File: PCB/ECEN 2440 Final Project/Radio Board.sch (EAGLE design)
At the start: 12 parts

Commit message: minor changes to board
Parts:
- added JP3: (no value), pinhead:PINHD-1X2
- added U$5: LDO-S-816, Custom Library:LDO-S-816
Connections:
- new net VCC: JP3.2, U$5.P$5
- net GND: now also JP3.1, U$5.P$2
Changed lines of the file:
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@@
 <part name="SJ1" library="jumper" library_urn="urn:adsk.eagle:library:252" deviceset="SJ" device="" package3d_urn="urn:adsk.eagle:package:15471/1"/>
 <part name="JP1" library="pinhead" library_urn="urn:adsk.eagle:library:325" deviceset="PINHD-1X1" device="" package3d_urn="urn:adsk.eagle:package:22485/2"/>
+<part name="U$5" library="Custom Library" deviceset="LDO-S-816" device=""/>
+<part name="GND16" library="supply1" library_urn="urn:adsk.eagle:library:371" deviceset="GND" device=""/>
+<part name="JP3" library="pinhead" library_urn="urn:adsk.eagle:library:325" deviceset="PINHD-1X2" device="" package3d_urn="urn:adsk.eagle:package:22435/2"/>
+<part name="GND2" library="supply1" library_urn="urn:adsk.eagle:library:371" deviceset="GND" device=""/>
+<part name="P+1" library="supply1" library_urn="urn:adsk.eagle:library:371" deviceset="VCC" device=""/>
 </parts>
 <sheets>
@@
 <attribute name="VALUE" x="95.25" y="12.7" size="1.778" layer="96"/>
 </instance>
+<instance part="U$5" gate="G$1" x="22.86" y="53.34" smashed="yes" rot="R90"/>
+<instance part="GND16" gate="1" x="30.48" y="68.58" smashed="yes" rot="R90">
+<attribute name="VALUE" x="33.02" y="66.04" size="1.778" layer="96" rot="R90"/>
+</instance>
+<instance part="JP3" gate="G$1" x="-38.1" y="73.66" smashed="yes" rot="R180">
+<attribute name="NAME" x="-31.75" y="67.945" size="1.778" layer="95" rot="R180"/>
+<attribute name="VALUE" x="-31.75" y="78.74" size="1.778" layer="96" rot="R180"/>
+</instance>
+<instance part="GND2" gate="1" x="-22.86" y="63.5" smashed="yes">
+<attribute name="VALUE" x="-25.4" y="60.96" size="1.778" layer="96"/>
+</instance>
+<instance part="P+1" gate="VCC" x="-25.4" y="76.2" smashed="yes">
+<attribute name="VALUE" x="-27.94" y="73.66" size="1.778" layer="96" rot="R90"/>
+</instance>
 </instances>
 <busses>
@@
 <pinref part="JP2" gate="A" pin="5"/>
 <pinref part="GND1" gate="1" pin="GND"/>
+</segment>
+<segment>
+<pinref part="U$5" gate="G$1" pin="P$2"/>
+<pinref part="GND16" gate="1" pin="GND"/>
+</segment>
+<segment>
+<pinref part="JP3" gate="G$1" pin="1"/>
+<wire x1="-35.56" y1="71.12" x2="-22.86" y2="71.12" width="0.1524" layer="91"/>
+<wire x1="-22.86" y1="71.12" x2="-22.86" y2="66.04" width="0.1524" layer="91"/>
+<pinref part="GND2" gate="1" pin="GND"/>
 </segment>
 </net>
@@
 </segment>
 </net>
+<net name="VCC" class="0">
+<segment>
+<pinref part="JP3" gate="G$1" pin="2"/>
+<pinref part="P+1" gate="VCC" pin="VCC"/>
+<wire x1="-35.56" y1="73.66" x2="-25.4" y2="73.66" width="0.1524" layer="91"/>
+<pinref part="U$5" gate="G$1" pin="P$5"/>
+<wire x1="-25.4" y1="73.66" x2="0" y2="73.66" width="0.1524" layer="91"/>
+<junction x="-25.4" y="73.66"/>
+</segment>
+</net>

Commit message: Final updates to the board
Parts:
- removed U$5: LDO-S-816, Custom Library:LDO-S-816
- added 3V3POWER: (no value), pinhead:PINHD-1X2
- added LM317: LM317, Custom Library:LM317
- added R4, R5: 100R, rcl:R-US_R0805
- renumbered JP2 to RADIO, JP3 to BATTERYPOWER
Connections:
- new net N$8: LM317.P$1, R4.1
- net +3V3: now also 3V3POWER.1, LM317.P$3, R4.2, R5.1
- net GND: now also 3V3POWER.2, R5.2; no longer U$5.P$2
- net VCC: now also LM317.P$2; no longer U$5.P$5
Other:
- note added: "LM317"
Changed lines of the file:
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@@
 <part name="GND12" library="supply1" library_urn="urn:adsk.eagle:library:371" deviceset="GND" device=""/>
 <part name="GND13" library="supply1" library_urn="urn:adsk.eagle:library:371" deviceset="GND" device=""/>
-<part name="JP2" library="pinhead" library_urn="urn:adsk.eagle:library:325" deviceset="PINHD-1X6" device="" package3d_urn="urn:adsk.eagle:package:22472/2"/>
+<part name="RADIO" library="pinhead" library_urn="urn:adsk.eagle:library:325" deviceset="PINHD-1X6" device="" package3d_urn="urn:adsk.eagle:package:22472/2"/>
 <part name="+3V1" library="supply1" library_urn="urn:adsk.eagle:library:371" deviceset="+3V3" device=""/>
 <part name="+3V2" library="supply1" library_urn="urn:adsk.eagle:library:371" deviceset="+3V3" device=""/>
@@
 <part name="SJ1" library="jumper" library_urn="urn:adsk.eagle:library:252" deviceset="SJ" device="" package3d_urn="urn:adsk.eagle:package:15471/1"/>
 <part name="JP1" library="pinhead" library_urn="urn:adsk.eagle:library:325" deviceset="PINHD-1X1" device="" package3d_urn="urn:adsk.eagle:package:22485/2"/>
-<part name="U$5" library="Custom Library" deviceset="LDO-S-816" device=""/>
-<part name="GND16" library="supply1" library_urn="urn:adsk.eagle:library:371" deviceset="GND" device=""/>
-<part name="JP3" library="pinhead" library_urn="urn:adsk.eagle:library:325" deviceset="PINHD-1X2" device="" package3d_urn="urn:adsk.eagle:package:22435/2"/>
+<part name="BATTERYPOWER" library="pinhead" library_urn="urn:adsk.eagle:library:325" deviceset="PINHD-1X2" device="" package3d_urn="urn:adsk.eagle:package:22435/2"/>
 <part name="GND2" library="supply1" library_urn="urn:adsk.eagle:library:371" deviceset="GND" device=""/>
 <part name="P+1" library="supply1" library_urn="urn:adsk.eagle:library:371" deviceset="VCC" device=""/>
+<part name="LM317" library="Custom Library" deviceset="LM317" device=""/>
+<part name="R4" library="rcl" library_urn="urn:adsk.eagle:library:334" deviceset="R-US_" device="R0805" package3d_urn="urn:adsk.eagle:package:23553/2" value="100R"/>
+<part name="R5" library="rcl" library_urn="urn:adsk.eagle:library:334" deviceset="R-US_" device="R0805" package3d_urn="urn:adsk.eagle:package:23553/2" value="100R"/>
+<part name="GND4" library="supply1" library_urn="urn:adsk.eagle:library:371" deviceset="GND" device=""/>
+<part name="3V3POWER" library="pinhead" library_urn="urn:adsk.eagle:library:325" deviceset="PINHD-1X2" device="" package3d_urn="urn:adsk.eagle:package:22435/2"/>
+<part name="GND5" library="supply1" library_urn="urn:adsk.eagle:library:371" deviceset="GND" device=""/>
+<part name="+3V3" library="supply1" library_urn="urn:adsk.eagle:library:371" deviceset="+3V3" device=""/>
 </parts>
 <sheets>
 <sheet>
 <plain>
+<text x="2.54" y="58.42" size="1.778" layer="91">LM317</text>
 </plain>
 <instances>
@@
 <attribute name="VALUE" x="137.16" y="66.04" size="1.778" layer="96" rot="R180"/>
 </instance>
-<instance part="JP2" gate="A" x="-12.7" y="33.02" smashed="yes" rot="R180">
+<instance part="RADIO" gate="A" x="-12.7" y="33.02" smashed="yes" rot="R180">
 <attribute name="NAME" x="-6.35" y="22.225" size="1.778" layer="95" rot="R180"/>
 <attribute name="VALUE" x="-6.35" y="43.18" size="1.778" layer="96" rot="R180"/>
@@
 <attribute name="VALUE" x="95.25" y="12.7" size="1.778" layer="96"/>
 </instance>
-<instance part="U$5" gate="G$1" x="22.86" y="53.34" smashed="yes" rot="R90"/>
-<instance part="GND16" gate="1" x="30.48" y="68.58" smashed="yes" rot="R90">
-<attribute name="VALUE" x="33.02" y="66.04" size="1.778" layer="96" rot="R90"/>
-</instance>
-<instance part="JP3" gate="G$1" x="-38.1" y="73.66" smashed="yes" rot="R180">
+<instance part="BATTERYPOWER" gate="G$1" x="-38.1" y="73.66" smashed="yes" rot="R180">
 <attribute name="NAME" x="-31.75" y="67.945" size="1.778" layer="95" rot="R180"/>
 <attribute name="VALUE" x="-31.75" y="78.74" size="1.778" layer="96" rot="R180"/>
@@
 <instance part="P+1" gate="VCC" x="-25.4" y="76.2" smashed="yes">
 <attribute name="VALUE" x="-27.94" y="73.66" size="1.778" layer="96" rot="R90"/>
+</instance>
+<instance part="LM317" gate="G$1" x="0" y="60.96" smashed="yes"/>
+<instance part="R4" gate="G$1" x="-5.08" y="86.36" smashed="yes" rot="R90">
+<attribute name="NAME" x="-6.5786" y="82.55" size="1.778" layer="95" rot="R90"/>
+<attribute name="VALUE" x="-1.778" y="82.55" size="1.778" layer="96" rot="R90"/>
+</instance>
+<instance part="R5" gate="G$1" x="-5.08" y="101.6" smashed="yes" rot="R90">
+<attribute name="NAME" x="-6.5786" y="97.79" size="1.778" layer="95" rot="R90"/>
+<attribute name="VALUE" x="-1.778" y="97.79" size="1.778" layer="96" rot="R90"/>
+</instance>
+<instance part="GND4" gate="1" x="-5.08" y="109.22" smashed="yes" rot="R180">
+<attribute name="VALUE" x="-2.54" y="111.76" size="1.778" layer="96" rot="R180"/>
+</instance>
+<instance part="3V3POWER" gate="G$1" x="33.02" y="68.58" smashed="yes">
+<attribute name="NAME" x="26.67" y="74.295" size="1.778" layer="95"/>
+<attribute name="VALUE" x="26.67" y="63.5" size="1.778" layer="96"/>
+</instance>
+<instance part="GND5" gate="1" x="25.4" y="63.5" smashed="yes">
+<attribute name="VALUE" x="22.86" y="60.96" size="1.778" layer="96"/>
+</instance>
+<instance part="+3V3" gate="G$1" x="22.86" y="73.66" smashed="yes">
+<attribute name="VALUE" x="20.32" y="68.58" size="1.778" layer="96" rot="R90"/>
 </instance>
 </instances>
@@
 </segment>
 <segment>
-<pinref part="JP2" gate="A" pin="2"/>
+<pinref part="RADIO" gate="A" pin="2"/>
 <wire x1="-10.16" y1="27.94" x2="-2.54" y2="27.94" width="0.1524" layer="91"/>
 <label x="-2.54" y="27.94" size="1.27" layer="95" xref="yes"/>
@@
 </segment>
 <segment>
-<pinref part="JP2" gate="A" pin="1"/>
+<pinref part="RADIO" gate="A" pin="1"/>
 <wire x1="-10.16" y1="25.4" x2="-2.54" y2="25.4" width="0.1524" layer="91"/>
 <label x="-2.54" y="25.4" size="1.27" layer="95" xref="yes"/>
@@
 </segment>
 <segment>
-<pinref part="JP2" gate="A" pin="4"/>
+<pinref part="RADIO" gate="A" pin="4"/>
 <wire x1="-10.16" y1="33.02" x2="-2.54" y2="33.02" width="0.1524" layer="91"/>
 <label x="-2.54" y="33.02" size="1.27" layer="95" xref="yes"/>
@@
 </segment>
 <segment>
-<pinref part="JP2" gate="A" pin="3"/>
+<pinref part="RADIO" gate="A" pin="3"/>
 <wire x1="-10.16" y1="30.48" x2="-2.54" y2="30.48" width="0.1524" layer="91"/>
 <label x="-2.54" y="30.48" size="1.27" layer="95" xref="yes"/>
@@
 </segment>
 <segment>
-<pinref part="JP2" gate="A" pin="5"/>
+<pinref part="RADIO" gate="A" pin="5"/>
 <pinref part="GND1" gate="1" pin="GND"/>
 </segment>
 <segment>
-<pinref part="U$5" gate="G$1" pin="P$2"/>
-<pinref part="GND16" gate="1" pin="GND"/>
-</segment>
-<segment>
-<pinref part="JP3" gate="G$1" pin="1"/>
+<pinref part="GND2" gate="1" pin="GND"/>
+<wire x1="-22.86" y1="71.12" x2="-22.86" y2="66.04" width="0.1524" layer="91"/>
+<pinref part="BATTERYPOWER" gate="G$1" pin="1"/>
 <wire x1="-35.56" y1="71.12" x2="-22.86" y2="71.12" width="0.1524" layer="91"/>
-<wire x1="-22.86" y1="71.12" x2="-22.86" y2="66.04" width="0.1524" layer="91"/>
-<pinref part="GND2" gate="1" pin="GND"/>
+</segment>
+<segment>
+<pinref part="R5" gate="G$1" pin="2"/>
+<pinref part="GND4" gate="1" pin="GND"/>
+</segment>
+<segment>
+<pinref part="3V3POWER" gate="G$1" pin="2"/>
+<wire x1="30.48" y1="68.58" x2="25.4" y2="68.58" width="0.1524" layer="91"/>
+<wire x1="25.4" y1="68.58" x2="25.4" y2="66.04" width="0.1524" layer="91"/>
+<pinref part="GND5" gate="1" pin="GND"/>
 </segment>
 </net>
@@
 </segment>
 <segment>
-<pinref part="JP2" gate="A" pin="6"/>
+<pinref part="RADIO" gate="A" pin="6"/>
 <pinref part="+3V2" gate="G$1" pin="+3V3"/>
+</segment>
+<segment>
+<pinref part="R5" gate="G$1" pin="1"/>
+<pinref part="R4" gate="G$1" pin="2"/>
+<wire x1="-5.08" y1="96.52" x2="-5.08" y2="91.44" width="0.1524" layer="91"/>
+<pinref part="LM317" gate="G$1" pin="P$3"/>
+<wire x1="-5.08" y1="91.44" x2="17.78" y2="91.44" width="0.1524" layer="91"/>
+<wire x1="17.78" y1="91.44" x2="17.78" y2="71.12" width="0.1524" layer="91"/>
+<junction x="-5.08" y="91.44"/>
+<pinref part="3V3POWER" gate="G$1" pin="1"/>
+<wire x1="30.48" y1="71.12" x2="22.86" y2="71.12" width="0.1524" layer="91"/>
+<junction x="17.78" y="71.12"/>
+<pinref part="+3V3" gate="G$1" pin="+3V3"/>
+<wire x1="22.86" y1="71.12" x2="17.78" y2="71.12" width="0.1524" layer="91"/>
+<junction x="22.86" y="71.12"/>
 </segment>
 </net>
@@
 <net name="VCC" class="0">
 <segment>
-<pinref part="JP3" gate="G$1" pin="2"/>
+<pinref part="BATTERYPOWER" gate="G$1" pin="2"/>
 <pinref part="P+1" gate="VCC" pin="VCC"/>
 <wire x1="-35.56" y1="73.66" x2="-25.4" y2="73.66" width="0.1524" layer="91"/>
-<pinref part="U$5" gate="G$1" pin="P$5"/>
-<wire x1="-25.4" y1="73.66" x2="0" y2="73.66" width="0.1524" layer="91"/>
+<wire x1="-25.4" y1="73.66" x2="-7.62" y2="73.66" width="0.1524" layer="91"/>
+<wire x1="-7.62" y1="73.66" x2="-7.62" y2="66.04" width="0.1524" layer="91"/>
 <junction x="-25.4" y="73.66"/>
-</segment>
-</net>
+<pinref part="LM317" gate="G$1" pin="P$2"/>
+<wire x1="-7.62" y1="66.04" x2="-5.08" y2="66.04" width="0.1524" layer="91"/>
+</segment>
+</net>
+<net name="N$8" class="0">
+<segment>
+<pinref part="R4" gate="G$1" pin="1"/>
+<pinref part="LM317" gate="G$1" pin="P$1"/>
+<wire x1="-5.08" y1="81.28" x2="-5.08" y2="76.2" width="0.1524" layer="91"/>
+</segment>
+</net>

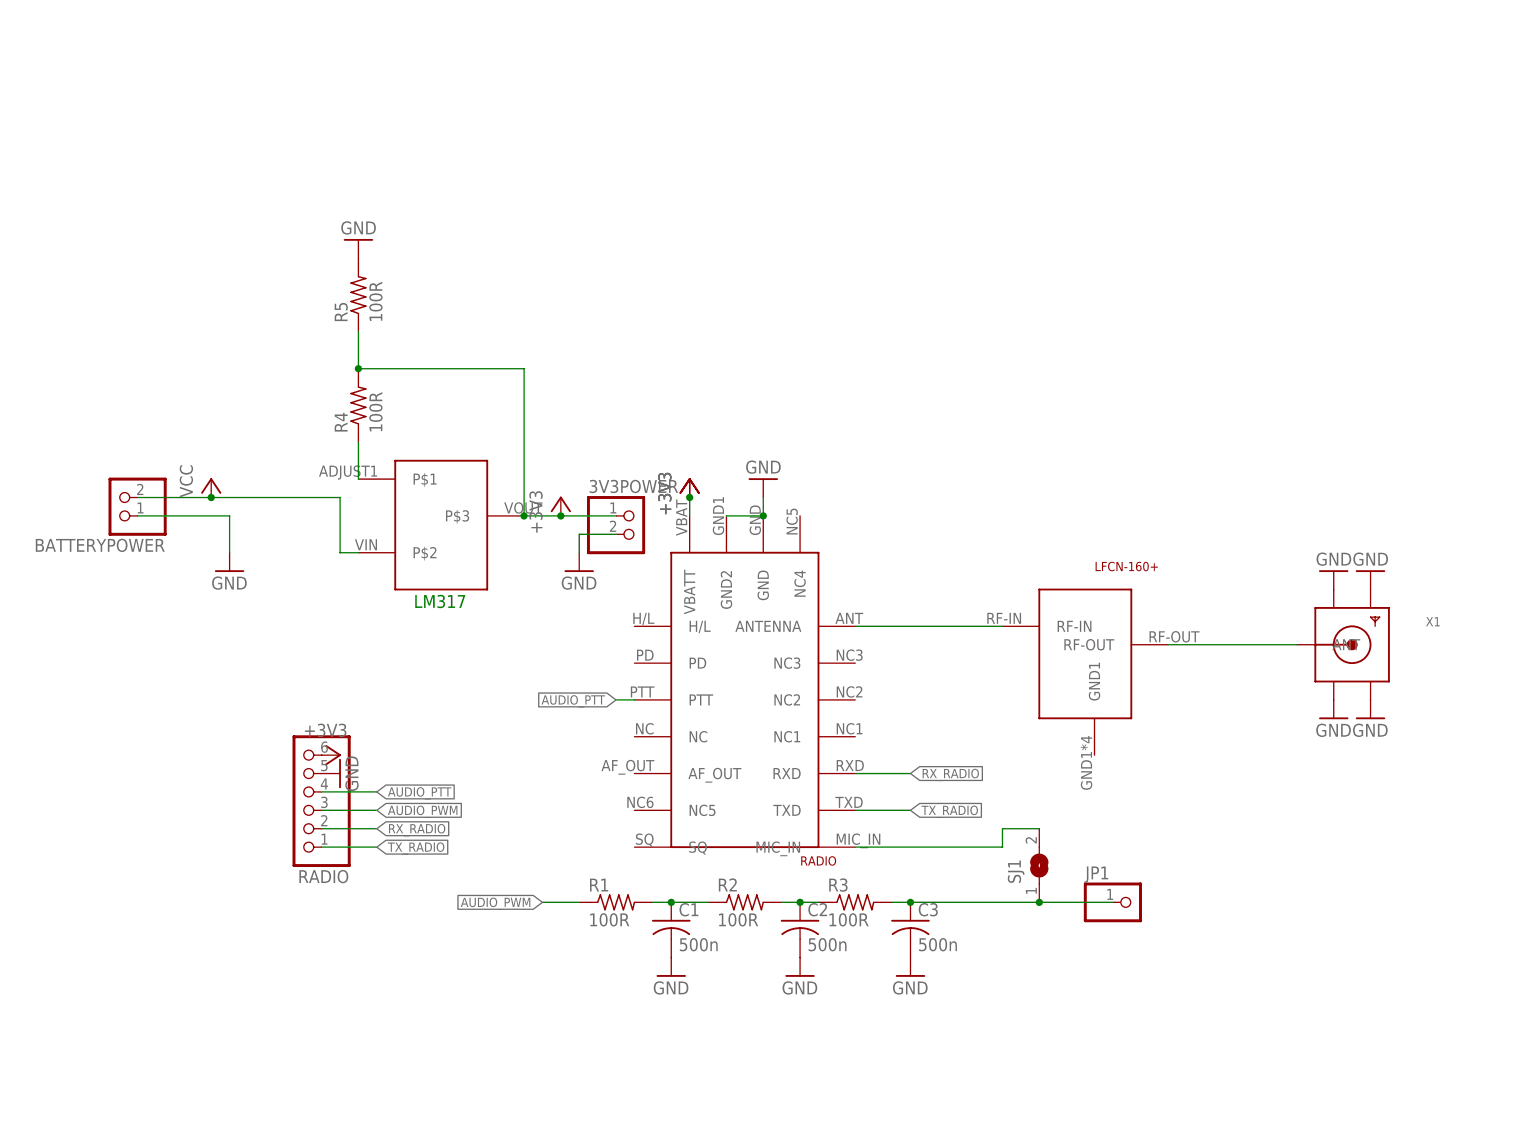
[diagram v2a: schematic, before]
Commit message: radio board routing
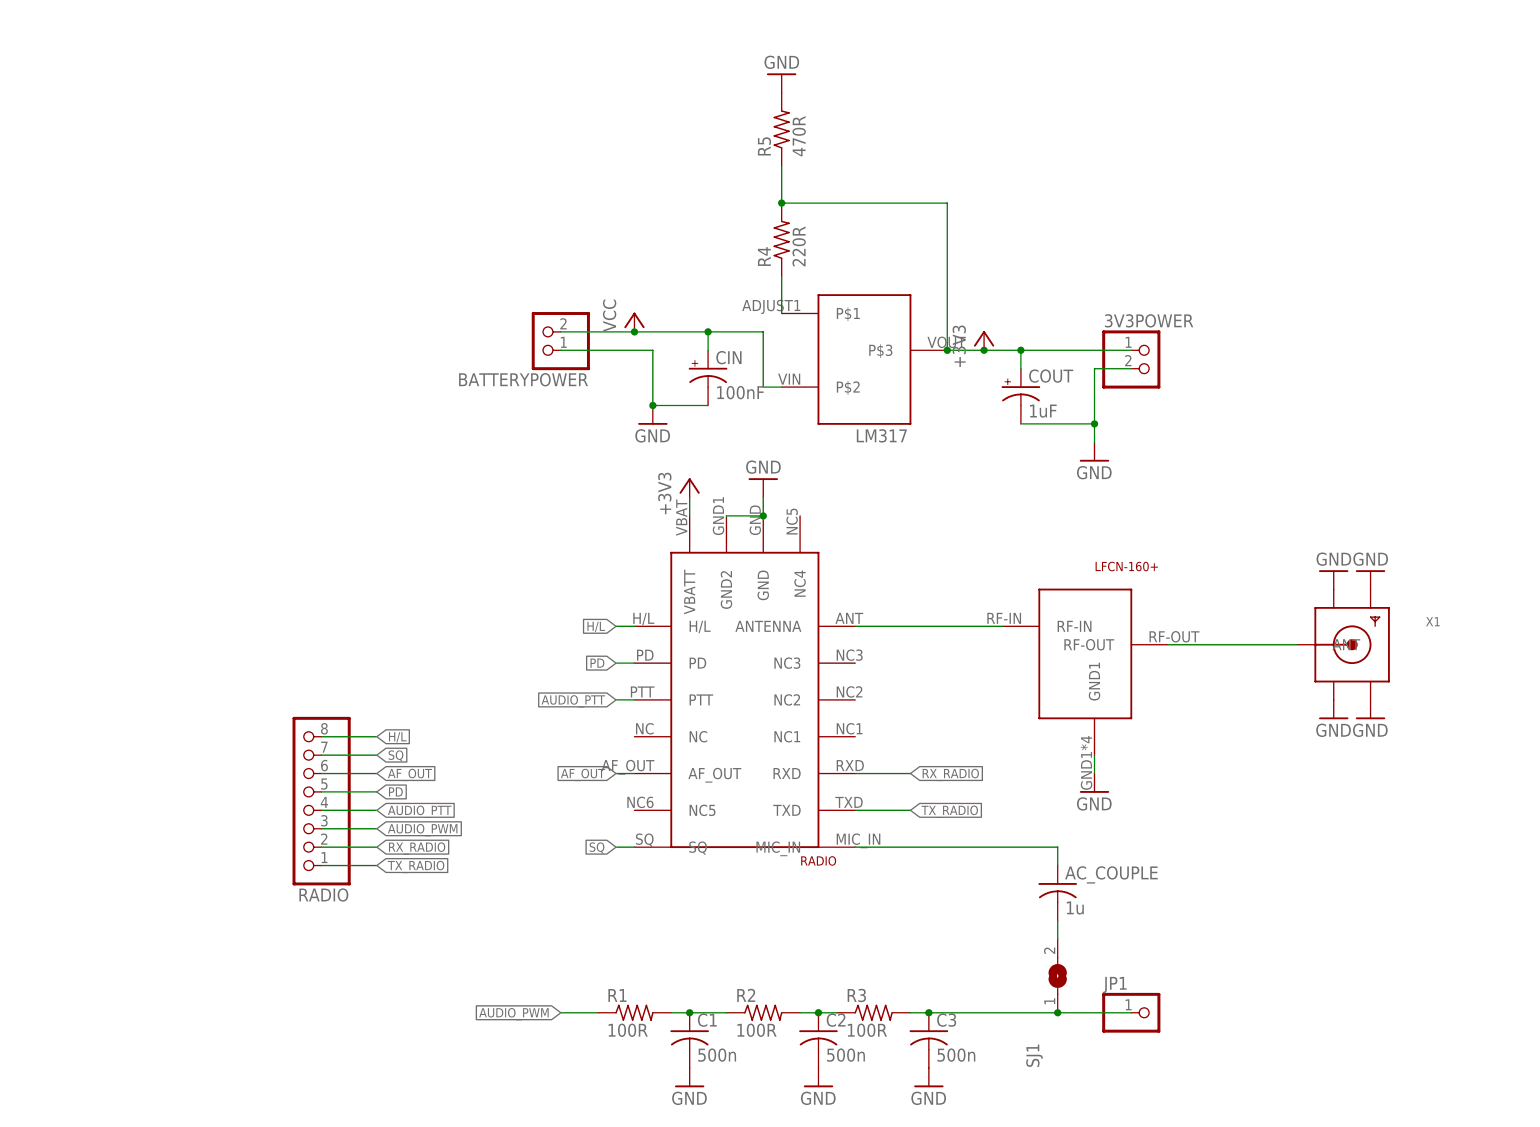
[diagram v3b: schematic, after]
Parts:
- added AC_COUPLE: 1u, rcl:C-USC0805
- added CIN: 100nF, rcl:CPOL-USA
- added COUT: 1uF, rcl:CPOL-USA
- R4: value 100R -> 220R
- R5: value 100R -> 470R
- RADIO: device pinhead:PINHD-1X6 -> pinhead:PINHD-1X8
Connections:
- new net AF_OUT: RADIO.6, U$4.AF_OUT
- new net H/L: RADIO.8, U$4.H/L
- new net N$7: AC_COUPLE.2, SJ1.2
- new net PD: RADIO.5, U$4.PD
- new net SQ: RADIO.7, U$4.SQ
- net +3V3: now also COUT.+; no longer RADIO.6
- net GND: now also CIN.-, COUT.-, U$6.GND1; no longer RADIO.5
- net N$5: now also AC_COUPLE.1; no longer SJ1.2
- net VCC: now also CIN.+
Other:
- moved on the sheet: 3V3POWER, BATTERYPOWER, C1, C2, C3, JP1, R1, R2, R3, R4, R5, SJ1

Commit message: final (before review & order) dra818v breakout board
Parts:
- renumbered BATTERYPOWER to BATT
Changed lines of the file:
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@@
 <part name="SJ1" library="jumper" library_urn="urn:adsk.eagle:library:252" deviceset="SJ" device="" package3d_urn="urn:adsk.eagle:package:15471/1"/>
 <part name="JP1" library="pinhead" library_urn="urn:adsk.eagle:library:325" deviceset="PINHD-1X1" device="" package3d_urn="urn:adsk.eagle:package:22485/2"/>
-<part name="BATTERYPOWER" library="pinhead" library_urn="urn:adsk.eagle:library:325" deviceset="PINHD-1X2" device="" package3d_urn="urn:adsk.eagle:package:22435/2"/>
+<part name="BATT" library="pinhead" library_urn="urn:adsk.eagle:library:325" deviceset="PINHD-1X2" device="" package3d_urn="urn:adsk.eagle:package:22435/2"/>
 <part name="GND2" library="supply1" library_urn="urn:adsk.eagle:library:371" deviceset="GND" device=""/>
 <part name="P+1" library="supply1" library_urn="urn:adsk.eagle:library:371" deviceset="VCC" device=""/>
@@
 <attribute name="VALUE" x="97.79" y="-2.54" size="1.778" layer="96"/>
 </instance>
-<instance part="BATTERYPOWER" gate="G$1" x="20.32" y="96.52" smashed="yes" rot="R180">
+<instance part="BATT" gate="G$1" x="20.32" y="96.52" smashed="yes" rot="R180">
 <attribute name="NAME" x="26.67" y="90.805" size="1.778" layer="95" rot="R180"/>
 <attribute name="VALUE" x="26.67" y="101.6" size="1.778" layer="96" rot="R180"/>
@@
 <pinref part="GND2" gate="1" pin="GND"/>
 <wire x1="35.56" y1="93.98" x2="35.56" y2="86.36" width="0.1524" layer="91"/>
-<pinref part="BATTERYPOWER" gate="G$1" pin="1"/>
+<pinref part="BATT" gate="G$1" pin="1"/>
 <wire x1="22.86" y1="93.98" x2="35.56" y2="93.98" width="0.1524" layer="91"/>
 <pinref part="CIN" gate="G$1" pin="-"/>
@@
 <net name="VCC" class="0">
 <segment>
-<pinref part="BATTERYPOWER" gate="G$1" pin="2"/>
+<pinref part="BATT" gate="G$1" pin="2"/>
 <pinref part="P+1" gate="VCC" pin="VCC"/>
 <wire x1="22.86" y1="96.52" x2="33.02" y2="96.52" width="0.1524" layer="91"/>
